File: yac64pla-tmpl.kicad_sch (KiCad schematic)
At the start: 3 parts, among them U1 GAL20V8_L, U2 GAL20V8_R, U3 C64_PLA

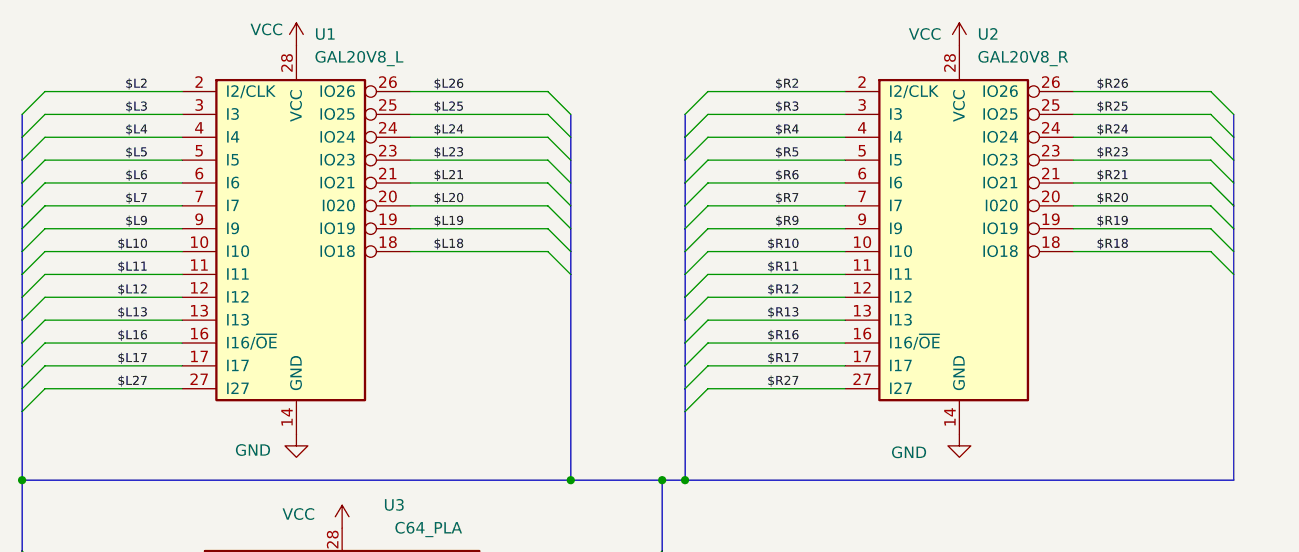
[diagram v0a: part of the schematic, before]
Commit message: Rename left/right to top/bottom
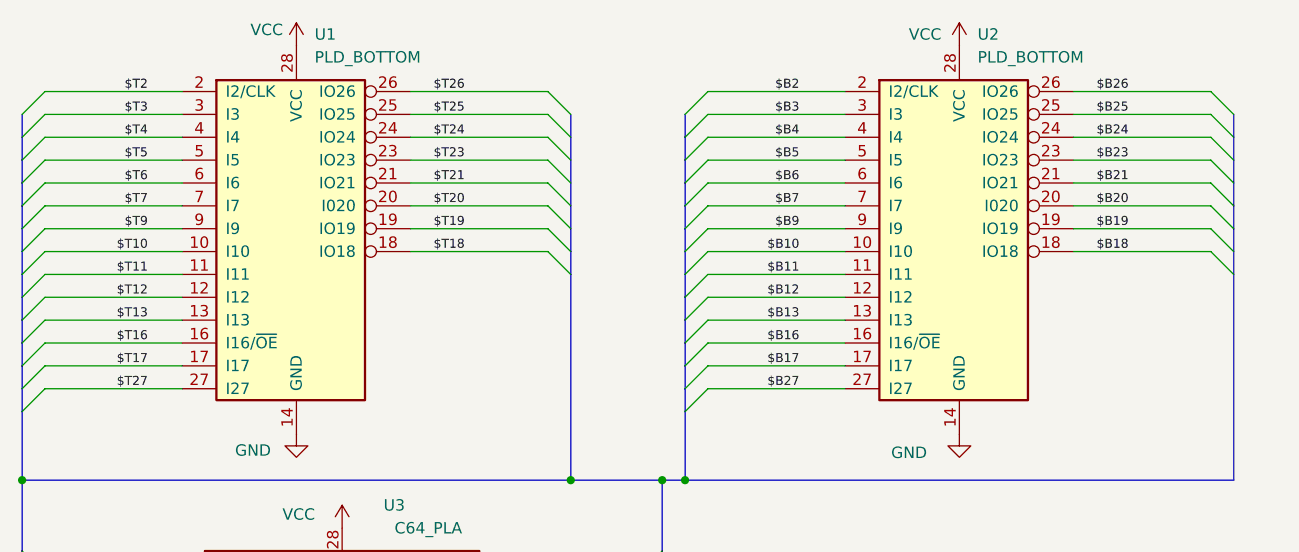
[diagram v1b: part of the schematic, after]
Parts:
- U1: value GAL20V8_L -> PLD_BOTTOM
- U2: value GAL20V8_R -> PLD_BOTTOM
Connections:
- net $L10 renamed $T10
- net $L11 renamed $T11
- net $L12 renamed $T12
- net $L13 renamed $T13
- net $L16 renamed $T16
- net $L17 renamed $T17
- net $L18 renamed $T18
- net $L19 renamed $T19
- net $L2 renamed $T2
- net $L20 renamed $T20
- net $L21 renamed $T21
- net $L23 renamed $T23
- net $L24 renamed $T24
- net $L25 renamed $T25
- net $L26 renamed $T26
- net $L27 renamed $T27
- net $L3 renamed $T3
- net $L4 renamed $T4
- net $L5 renamed $T5
- net $L6 renamed $T6
- net $L7 renamed $T7
- net $L9 renamed $T9
- net $R10 renamed $B10
- net $R11 renamed $B11
- net $R12 renamed $B12
- net $R13 renamed $B13
- net $R16 renamed $B16
- net $R17 renamed $B17
- net $R18 renamed $B18
- net $R19 renamed $B19
- net $R2 renamed $B2
- net $R20 renamed $B20
- net $R21 renamed $B21
- net $R23 renamed $B23
- net $R24 renamed $B24
- net $R25 renamed $B25
- net $R26 renamed $B26
- net $R27 renamed $B27
- net $R3 renamed $B3
- net $R4 renamed $B4
- net $R5 renamed $B5
- net $R6 renamed $B6
- net $R7 renamed $B7
- net $R9 renamed $B9
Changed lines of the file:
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@@
     (stroke (width 0) (type default) (color 0 0 0 0))
   )
-  (label "$L2" (at 39.37 23.622 180)
-    (effects (font (size 1 1)) (justify right bottom))
-  )
-  (label "$R18" (at 144.78 41.402 0)
-    (effects (font (size 1 1)) (justify left bottom))
-  )
-  (label "$R23" (at 144.78 31.242 0)
+  (label "$T2" (at 39.37 23.622 180)
+    (effects (font (size 1 1)) (justify right bottom))
+  )
+  (label "$B18" (at 144.78 41.402 0)
+    (effects (font (size 1 1)) (justify left bottom))
+  )
+  (label "$B23" (at 144.78 31.242 0)
     (effects (font (size 1 1)) (justify left bottom))
   )
@@
     (effects (font (size 1 1)) (justify left bottom))
   )
-  (label "$R16" (at 111.76 51.562 180)
-    (effects (font (size 1 1)) (justify right bottom))
-  )
-  (label "$L19" (at 71.12 38.862 0)
-    (effects (font (size 1 1)) (justify left bottom))
-  )
-  (label "$L23" (at 71.12 31.242 0)
+  (label "$B16" (at 111.76 51.562 180)
+    (effects (font (size 1 1)) (justify right bottom))
+  )
+  (label "$T19" (at 71.12 38.862 0)
+    (effects (font (size 1 1)) (justify left bottom))
+  )
+  (label "$T23" (at 71.12 31.242 0)
     (effects (font (size 1 1)) (justify left bottom))
   )
@@
     (effects (font (size 1 1)) (justify right bottom))
   )
-  (label "$L18" (at 71.12 41.402 0)
+  (label "$T18" (at 71.12 41.402 0)
     (effects (font (size 1 1)) (justify left bottom))
   )
@@
     (effects (font (size 1 1)) (justify right bottom))
   )
-  (label "$R3" (at 111.76 26.162 180)
-    (effects (font (size 1 1)) (justify right bottom))
-  )
-  (label "$R19" (at 144.78 38.862 0)
-    (effects (font (size 1 1)) (justify left bottom))
-  )
-  (label "$L10" (at 39.37 41.402 180)
-    (effects (font (size 1 1)) (justify right bottom))
-  )
-  (label "$R4" (at 111.76 28.702 180)
+  (label "$B3" (at 111.76 26.162 180)
+    (effects (font (size 1 1)) (justify right bottom))
+  )
+  (label "$B19" (at 144.78 38.862 0)
+    (effects (font (size 1 1)) (justify left bottom))
+  )
+  (label "$T10" (at 39.37 41.402 180)
+    (effects (font (size 1 1)) (justify right bottom))
+  )
+  (label "$B4" (at 111.76 28.702 180)
     (effects (font (size 1 1)) (justify right bottom))
   )
@@
     (effects (font (size 1 1)) (justify left bottom))
   )
-  (label "$R12" (at 111.76 46.482 180)
-    (effects (font (size 1 1)) (justify right bottom))
-  )
-  (label "$R20" (at 144.78 36.322 0)
-    (effects (font (size 1 1)) (justify left bottom))
-  )
-  (label "$R7" (at 111.76 36.322 180)
+  (label "$B12" (at 111.76 46.482 180)
+    (effects (font (size 1 1)) (justify right bottom))
+  )
+  (label "$B20" (at 144.78 36.322 0)
+    (effects (font (size 1 1)) (justify left bottom))
+  )
+  (label "$B7" (at 111.76 36.322 180)
     (effects (font (size 1 1)) (justify right bottom))
   )
@@
     (effects (font (size 1 1)) (justify right bottom))
   )
-  (label "$L25" (at 71.12 26.162 0)
+  (label "$T25" (at 71.12 26.162 0)
     (effects (font (size 1 1)) (justify left bottom))
   )
@@
     (effects (font (size 1 1)) (justify right bottom))
   )
-  (label "$R21" (at 144.78 33.782 0)
-    (effects (font (size 1 1)) (justify left bottom))
-  )
-  (label "$R10" (at 111.76 41.402 180)
-    (effects (font (size 1 1)) (justify right bottom))
-  )
-  (label "$L20" (at 71.12 36.322 0)
-    (effects (font (size 1 1)) (justify left bottom))
-  )
-  (label "$L16" (at 39.37 51.562 180)
-    (effects (font (size 1 1)) (justify right bottom))
-  )
-  (label "$L9" (at 39.37 38.862 180)
+  (label "$B21" (at 144.78 33.782 0)
+    (effects (font (size 1 1)) (justify left bottom))
+  )
+  (label "$B10" (at 111.76 41.402 180)
+    (effects (font (size 1 1)) (justify right bottom))
+  )
+  (label "$T20" (at 71.12 36.322 0)
+    (effects (font (size 1 1)) (justify left bottom))
+  )
+  (label "$T16" (at 39.37 51.562 180)
+    (effects (font (size 1 1)) (justify right bottom))
+  )
+  (label "$T9" (at 39.37 38.862 180)
     (effects (font (size 1 1)) (justify right bottom))
   )
@@
     (effects (font (size 1 1)) (justify left bottom))
   )
-  (label "$L12" (at 39.37 46.482 180)
-    (effects (font (size 1 1)) (justify right bottom))
-  )
-  (label "$R11" (at 111.76 43.942 180)
-    (effects (font (size 1 1)) (justify right bottom))
-  )
-  (label "$L3" (at 39.37 26.162 180)
-    (effects (font (size 1 1)) (justify right bottom))
-  )
-  (label "$R2" (at 111.76 23.622 180)
-    (effects (font (size 1 1)) (justify right bottom))
-  )
-  (label "$L17" (at 39.37 54.102 180)
+  (label "$T12" (at 39.37 46.482 180)
+    (effects (font (size 1 1)) (justify right bottom))
+  )
+  (label "$B11" (at 111.76 43.942 180)
+    (effects (font (size 1 1)) (justify right bottom))
+  )
+  (label "$T3" (at 39.37 26.162 180)
+    (effects (font (size 1 1)) (justify right bottom))
+  )
+  (label "$B2" (at 111.76 23.622 180)
+    (effects (font (size 1 1)) (justify right bottom))
+  )
+  (label "$T17" (at 39.37 54.102 180)
     (effects (font (size 1 1)) (justify right bottom))
   )
@@
     (effects (font (size 1 1)) (justify left bottom))
   )
-  (label "$L5" (at 39.37 31.242 180)
+  (label "$T5" (at 39.37 31.242 180)
     (effects (font (size 1 1)) (justify right bottom))
   )
@@
     (effects (font (size 1 1)) (justify left bottom))
   )
-  (label "$L27" (at 39.37 56.642 180)
-    (effects (font (size 1 1)) (justify right bottom))
-  )
-  (label "$R25" (at 144.78 26.162 0)
+  (label "$T27" (at 39.37 56.642 180)
+    (effects (font (size 1 1)) (justify right bottom))
+  )
+  (label "$B25" (at 144.78 26.162 0)
     (effects (font (size 1 1)) (justify left bottom))
   )
@@
     (effects (font (size 1 1)) (justify right bottom))
   )
-  (label "$L24" (at 71.12 28.702 0)
-    (effects (font (size 1 1)) (justify left bottom))
-  )
-  (label "$R5" (at 111.76 31.242 180)
-    (effects (font (size 1 1)) (justify right bottom))
-  )
-  (label "$L21" (at 71.12 33.782 0)
+  (label "$T24" (at 71.12 28.702 0)
+    (effects (font (size 1 1)) (justify left bottom))
+  )
+  (label "$B5" (at 111.76 31.242 180)
+    (effects (font (size 1 1)) (justify right bottom))
+  )
+  (label "$T21" (at 71.12 33.782 0)
     (effects (font (size 1 1)) (justify left bottom))
   )
@@
     (effects (font (size 1 1)) (justify right bottom))
   )
-  (label "$L7" (at 39.37 36.322 180)
+  (label "$T7" (at 39.37 36.322 180)
     (effects (font (size 1 1)) (justify right bottom))
   )
@@
     (effects (font (size 1 1)) (justify right bottom))
   )
-  (label "$R27" (at 111.76 56.642 180)
-    (effects (font (size 1 1)) (justify right bottom))
-  )
-  (label "$R9" (at 111.76 38.862 180)
+  (label "$B27" (at 111.76 56.642 180)
+    (effects (font (size 1 1)) (justify right bottom))
+  )
+  (label "$B9" (at 111.76 38.862 180)
     (effects (font (size 1 1)) (justify right bottom))
   )
@@
     (effects (font (size 1 1)) (justify right bottom))
   )
-  (label "$R13" (at 111.76 49.022 180)
+  (label "$B13" (at 111.76 49.022 180)
     (effects (font (size 1 1)) (justify right bottom))
   )
@@
     (effects (font (size 1 1)) (justify right bottom))
   )
-  (label "$R26" (at 144.78 23.622 0)
+  (label "$B26" (at 144.78 23.622 0)
     (effects (font (size 1 1)) (justify left bottom))
   )
@@
     (effects (font (size 1 1)) (justify right bottom))
   )
-  (label "$R6" (at 111.76 33.782 180)
-    (effects (font (size 1 1)) (justify right bottom))
-  )
-  (label "$L13" (at 39.37 49.022 180)
-    (effects (font (size 1 1)) (justify right bottom))
-  )
-  (label "$R17" (at 111.76 54.102 180)
-    (effects (font (size 1 1)) (justify right bottom))
-  )
-  (label "$L11" (at 39.37 43.942 180)
-    (effects (font (size 1 1)) (justify right bottom))
-  )
-  (label "$L26" (at 71.12 23.622 0)
+  (label "$B6" (at 111.76 33.782 180)
+    (effects (font (size 1 1)) (justify right bottom))
+  )
+  (label "$T13" (at 39.37 49.022 180)
+    (effects (font (size 1 1)) (justify right bottom))
+  )
+  (label "$B17" (at 111.76 54.102 180)
+    (effects (font (size 1 1)) (justify right bottom))
+  )
+  (label "$T11" (at 39.37 43.942 180)
+    (effects (font (size 1 1)) (justify right bottom))
+  )
+  (label "$T26" (at 71.12 23.622 0)
     (effects (font (size 1 1)) (justify left bottom))
   )
@@
     (effects (font (size 1 1)) (justify right bottom))
   )
-  (label "$L6" (at 39.37 33.782 180)
-    (effects (font (size 1 1)) (justify right bottom))
-  )
-  (label "$L4" (at 39.37 28.702 180)
+  (label "$T6" (at 39.37 33.782 180)
+    (effects (font (size 1 1)) (justify right bottom))
+  )
+  (label "$T4" (at 39.37 28.702 180)
     (effects (font (size 1 1)) (justify right bottom))
   )
@@
     (effects (font (size 1 1)) (justify right bottom))
   )
-  (label "$R24" (at 144.78 28.702 0)
+  (label "$B24" (at 144.78 28.702 0)
     (effects (font (size 1 1)) (justify left bottom))
   )
@@
       (effects (font (size 1.27 1.27)) (justify left))
     )
-    (property "Value" "GAL20V8_R" (id 1) (at 131.5594 19.812 0)
+    (property "Value" "PLD_BOTTOM" (id 1) (at 131.5594 19.812 0)
       (effects (font (size 1.27 1.27)) (justify left))
     )
@@
       (effects (font (size 1.27 1.27)) (justify left))
     )
-    (property "Value" "GAL20V8_L" (id 1) (at 57.8994 19.812 0)
+    (property "Value" "PLD_BOTTOM" (id 1) (at 57.8994 19.812 0)
       (effects (font (size 1.27 1.27)) (justify left))
     )
@@
     )
     (path "/e092c7ae-5dc4-42e1-9b43-28f40f25cebf"
-      (reference "U1") (unit 1) (value "GAL20V8_L") (footprint "Package_LCC:PLCC-28")
+      (reference "U1") (unit 1) (value "PLD_TOP") (footprint "Package_LCC:PLCC-28")
     )
     (path "/b0e14891-ade3-41a8-a1ed-ca5b421cb573"
-      (reference "U2") (unit 1) (value "GAL20V8_R") (footprint "Package_LCC:PLCC-28")
+      (reference "U2") (unit 1) (value "PLD_BOTTOM") (footprint "Package_LCC:PLCC-28")
     )
     (path "/851e7b1c-259f-42bc-9440-0054649e3241"
